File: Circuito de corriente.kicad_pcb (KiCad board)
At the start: 2 copper layers, 150 x 120 mm, 110 parts, among them J1 SALIDAS, J2 ENTRADAS, J3 +12V2, J4 +3V3, J5 +/- 5V, J6 +/- 12V, J7 INPUT_CEDCp, K1 JJM1-12V, K2 JJM1-12V, K3 JJM1-12V, K4 SLA-12VDC-SL-C, M1 Fan_3pin, Q1 BC337, Q2 BC327, U1 OPA604, U13 LM35-NEB, U16 Fuse, U18 IRLZ44N, U2 OPA604, U20 IRLZ44N, U22 IRLZ44N, U3 A6841, U4 AD7606_M, U5 MCP4725, U55 IRLZ44N, U6 OPA604, U7 OPA604, U8 OPA604

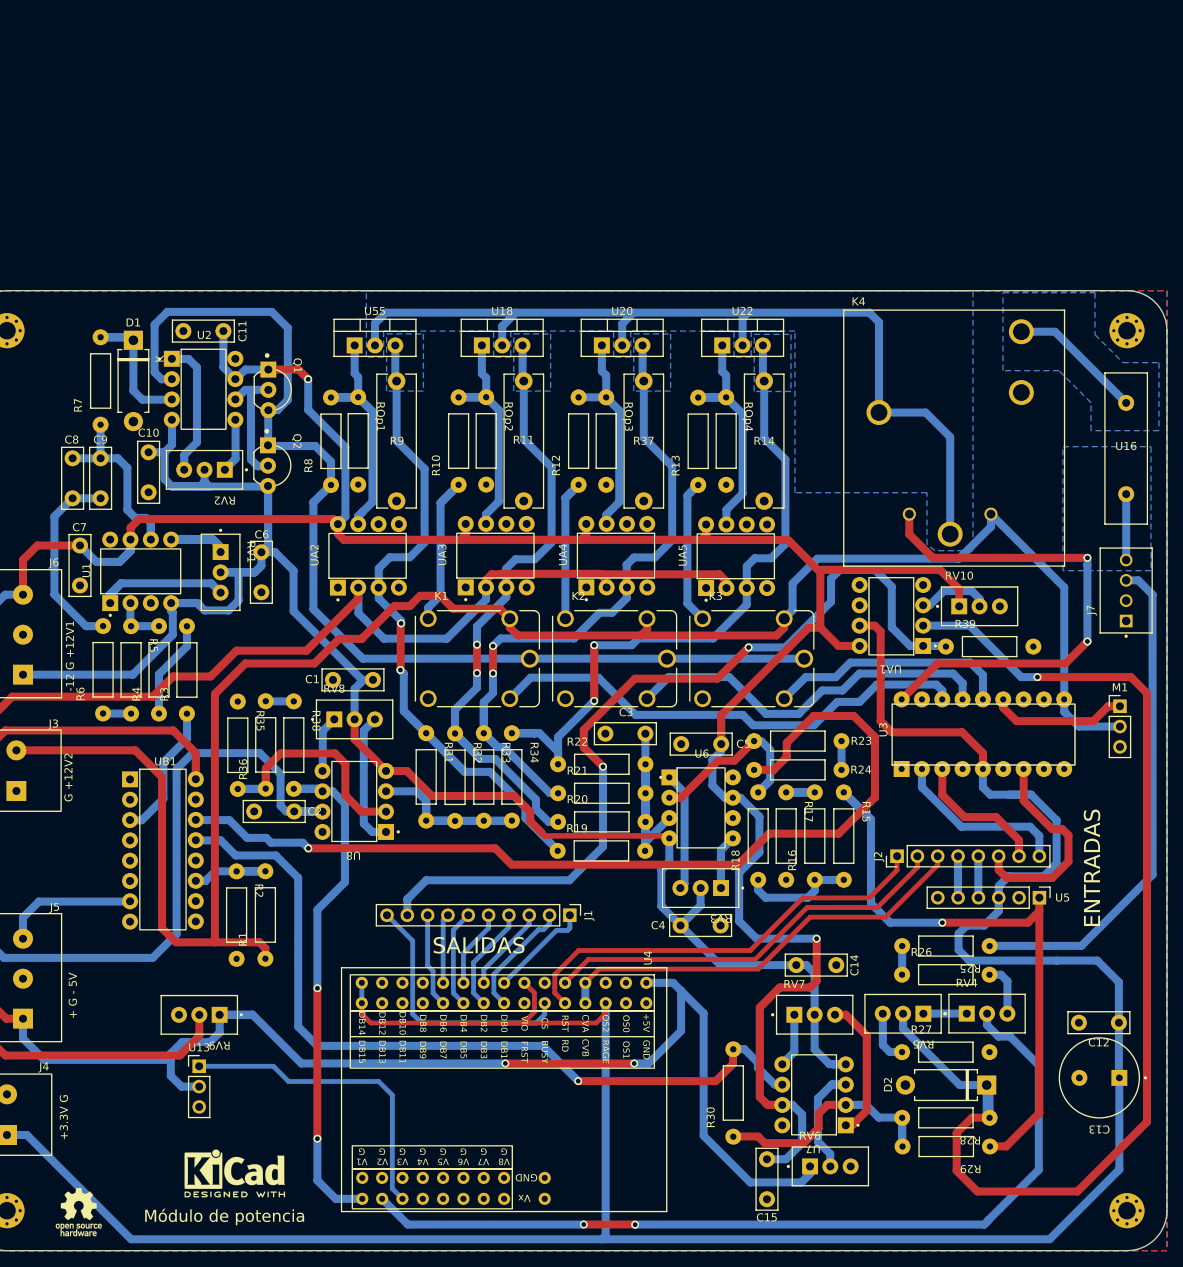
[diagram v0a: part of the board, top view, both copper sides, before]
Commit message: Heat sink added + Large pads
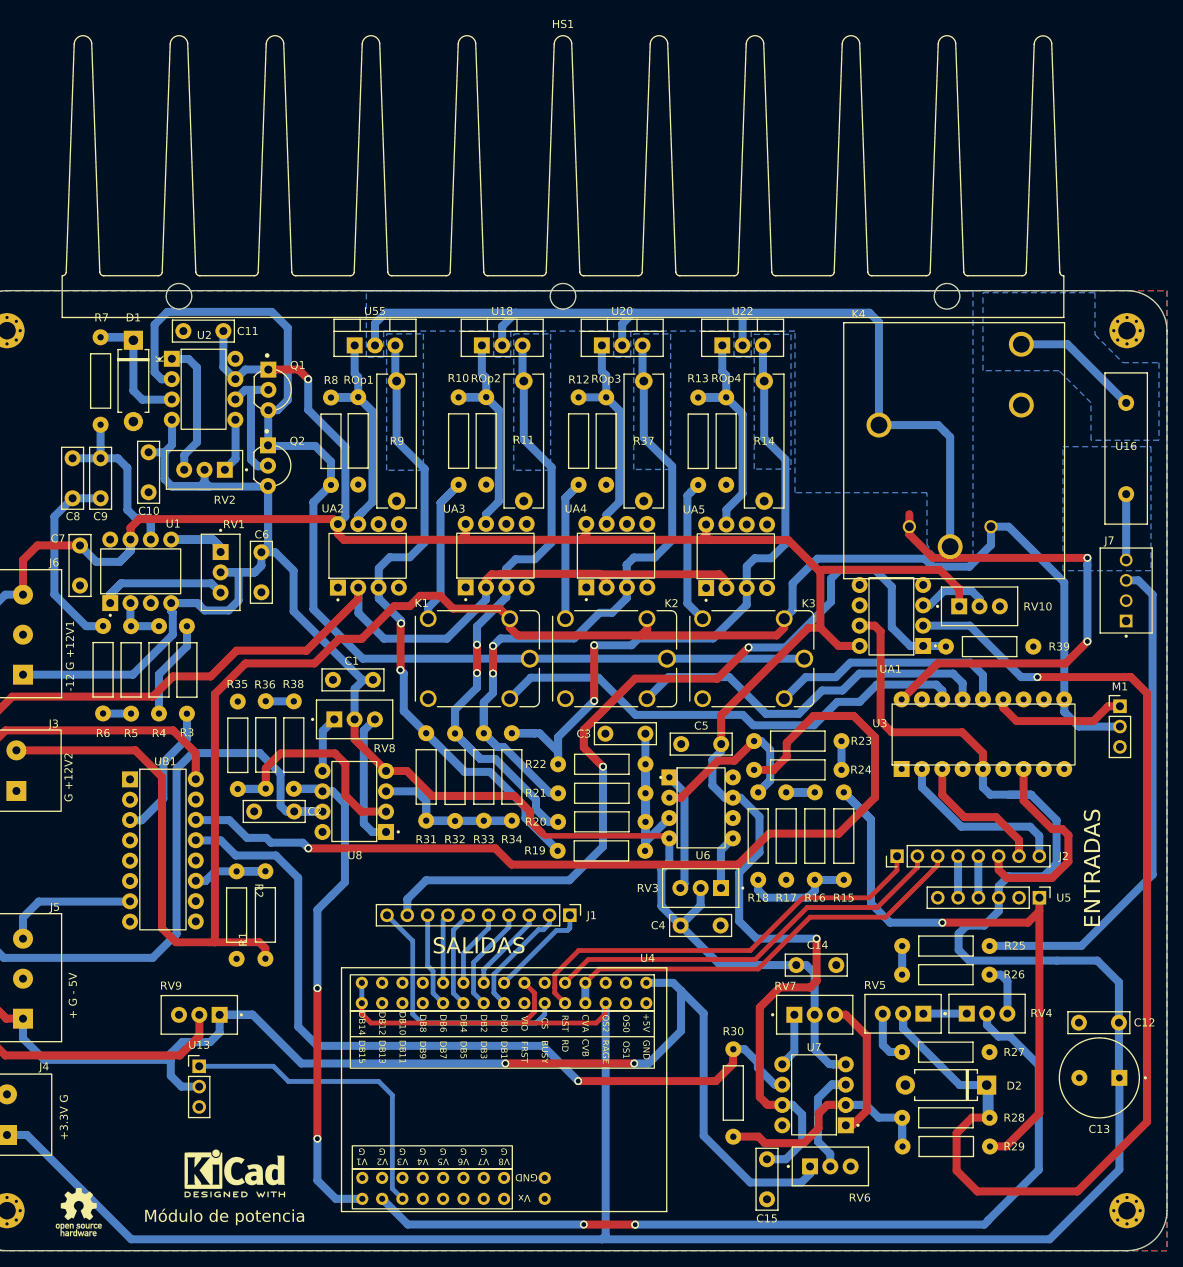
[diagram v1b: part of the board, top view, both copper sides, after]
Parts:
- added HS1: Heatsink, Heatsink:Heatsink_125x35x50mm_3xFixationM3, F.Cu at (139.7, 28.4)
- moved K4 1.57 mm to (188.1, 42.0)
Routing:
- net /CEP_Input+_MOS: track 114.2 -> 115.2 mm
- net /Proteccion Sobre Tension (53V)/F_In: track 16.8 -> 16.1 mm

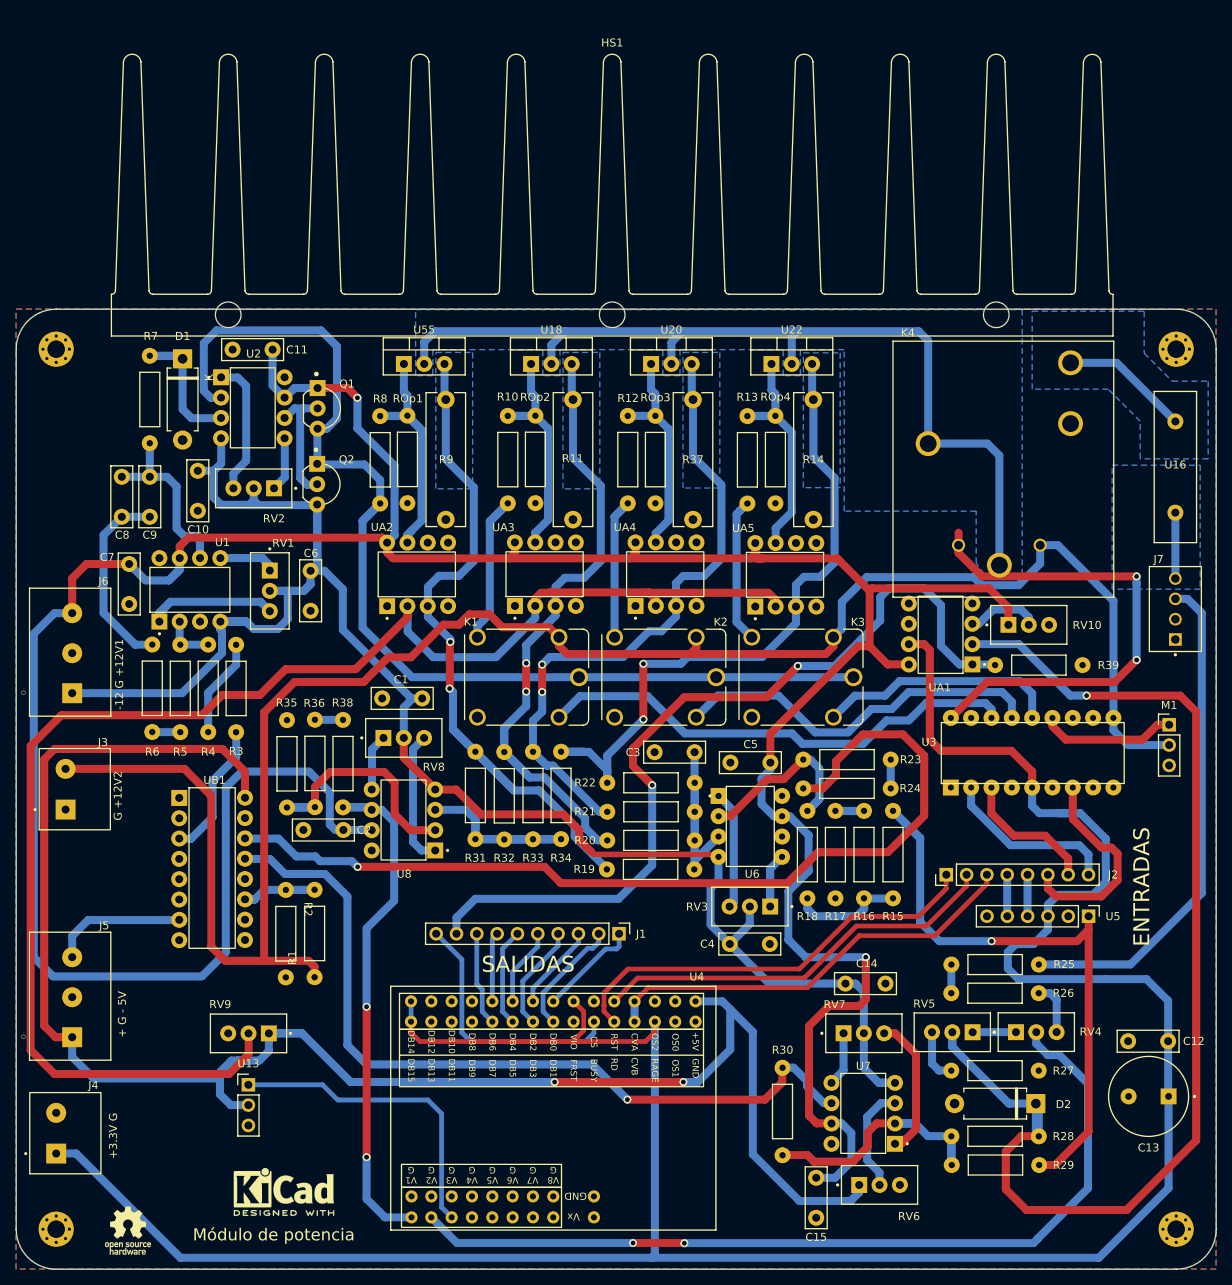
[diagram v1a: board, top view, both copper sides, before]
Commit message: Pads mas grandes y correccion de vias
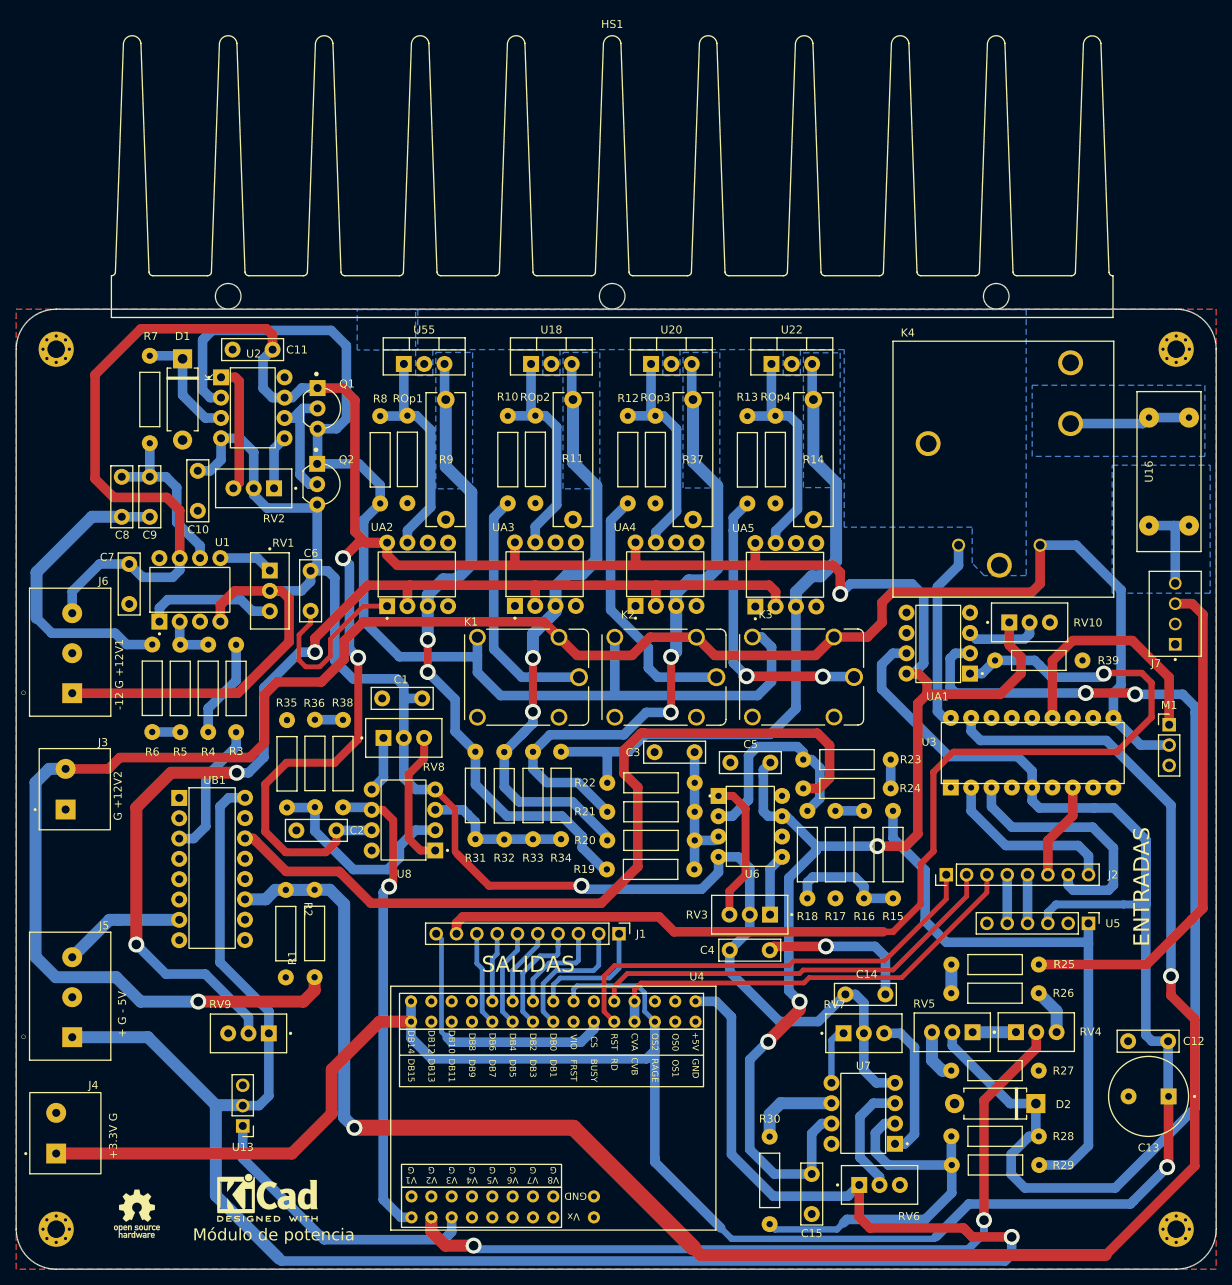
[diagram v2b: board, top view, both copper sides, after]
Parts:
- U16: footprint Fuse:Fuse_Littelfuse-LVR100 -> CEDCp:Fuse
- moved R30 8.76 mm to (159.4, 136.6)
- moved U13 5.19 mm to (93.5, 129.8), turned to 180 degrees
- moved U16 3.67 mm to (206.8, 54.8)
- moved REF** 2.39 mm to (80.3, 140.8)
- moved HS1 2.31 mm to (139.7, 26.1)
- moved REF** 2.20 mm to (96.6, 138.8)
- moved C14 1.35 mm to (173.8, 113.3)
- moved UA1 1.18 mm to (180.5, 69.4)
- moved RV3 1.01 mm to (156.9, 103.4)
- moved U5 0.89 mm to (199.2, 104.5)
- moved C2 0.88 mm to (100.2, 92.8)
- moved C4 0.77 mm to (154.4, 107.8)
- moved C15 0.73 mm to (164.6, 140.8)
- moved J7 0.60 mm to (210.1, 69.6)
- moved R39 0.59 mm to (193.0, 71.6)
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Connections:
- K1 pad 3: Net-(K1-Pad3) -> /PushPullOut
- K1 pad 5: /PushPullOut -> Net-(K1-Pad5)
- K2 pad 3: Net-(K2-Pad3) -> /PushPullOut
- K2 pad 5: /PushPullOut -> Net-(R12-Pad1)
- K3 pad 3: Net-(K3-Pad3) -> /PushPullOut
- K3 pad 5: /PushPullOut -> Net-(R13-Pad1)
- K4 pad NC: /Proteccion Sobre Tension (53V)/F_In -> unconnected-(K4-PadNC)
- K4 pad NO: GND -> /Proteccion Sobre Tension (53V)/F_In
- R1 pad 2: /fromMicroC_FBLSelection -> /fromA6841_FeedbackLoopSelection
- R10 pad 1: Net-(K1-Pad3) -> Net-(K1-Pad5)
- R12 pad 1: Net-(K2-Pad3) -> Net-(R12-Pad1)
- R13 pad 1: Net-(K3-Pad3) -> Net-(R13-Pad1)
- R2 pad 1: /fromMicroC_FBLSelection -> /fromA6841_FeedbackLoopSelection
- UB1 pad 11: /fromMicroC_FBLSelection -> /fromA6841_FeedbackLoopSelection
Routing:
- net /fromA6841_FeedbackLoopSelection: track 0.00 -> 261.4 mm, vias 0 -> 2
- net /CEP_Input+_MOS: track 115.2 -> 0.00 mm
- net /Error2: track 101.6 -> 11.1 mm, vias 1 -> 0
- net Net-(K1-Pad2): track 61.1 -> 0.00 mm
- net Net-(U3-Pad15): track 47.1 -> 0.00 mm
- net GND: track 0.00 -> 46.1 mm, vias 0 -> 1
- net /+5V: track 220.4 -> 260.0 mm, vias 2 -> 1
- net /ILimit_Vref: track 183.9 -> 144.6 mm, vias 0 -> 4
- net /fromA6841_PowerEnable: track 62.7 -> 23.9 mm, vias 2 -> 0
- net Net-(R13-Pad1): track 0.00 -> 36.5 mm, vias 0 -> 2
- net /toMicroC_OverVoltageSignal: track 107.0 -> 140.7 mm, vias 2 -> 1
- net Net-(R12-Pad1): track 0.00 -> 32.4 mm
- net Net-(K1-Pad5): track 0.00 -> 31.1 mm
- net Net-(U3-Pad14): track 30.4 -> 0.00 mm
- net Net-(K1-Pad3): track 21.5 -> 0.00 mm
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
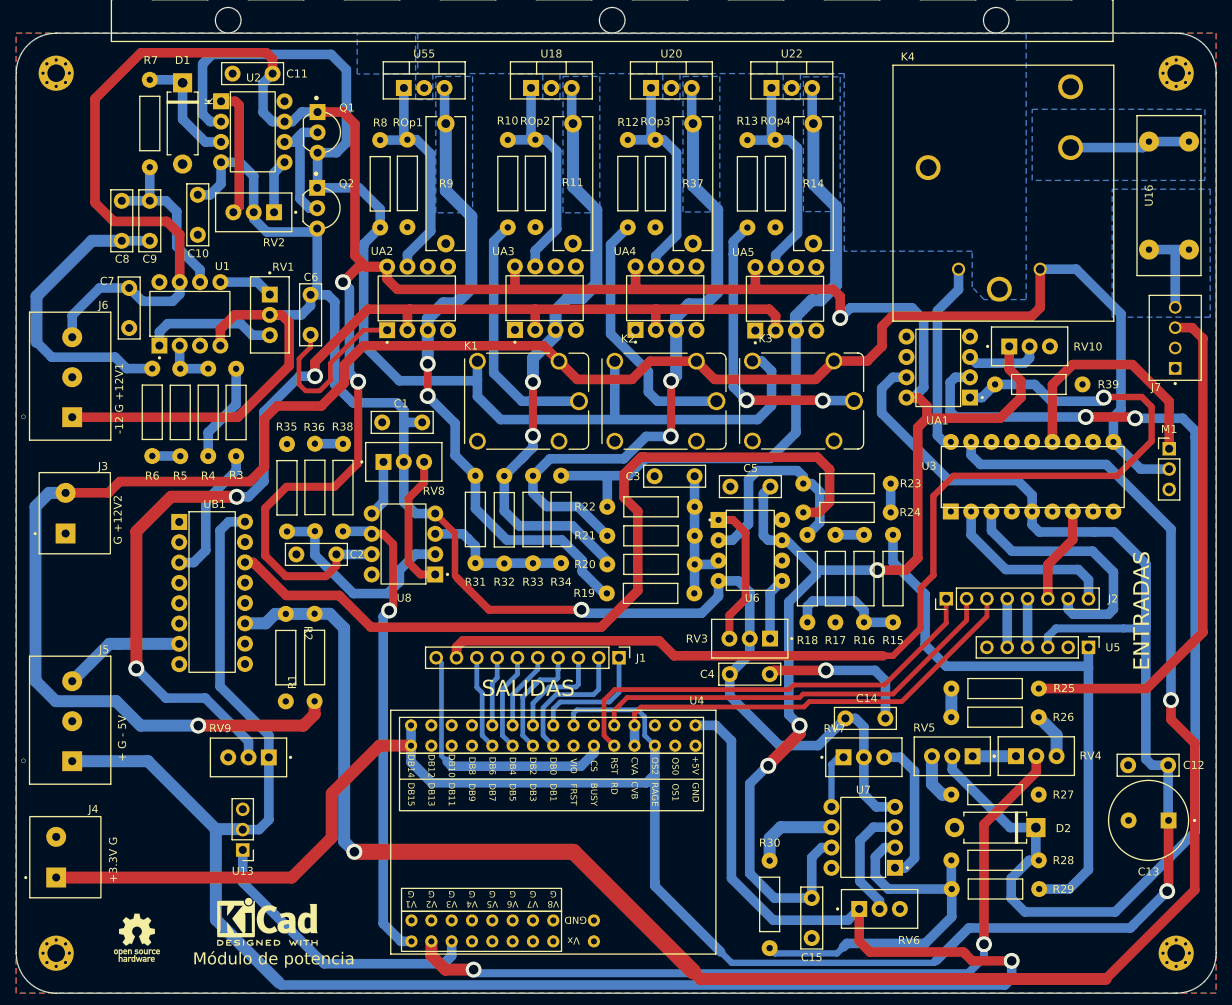
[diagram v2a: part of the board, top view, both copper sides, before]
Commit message: Se agrandaron los pads de las VIAS y ensancharon las pistas
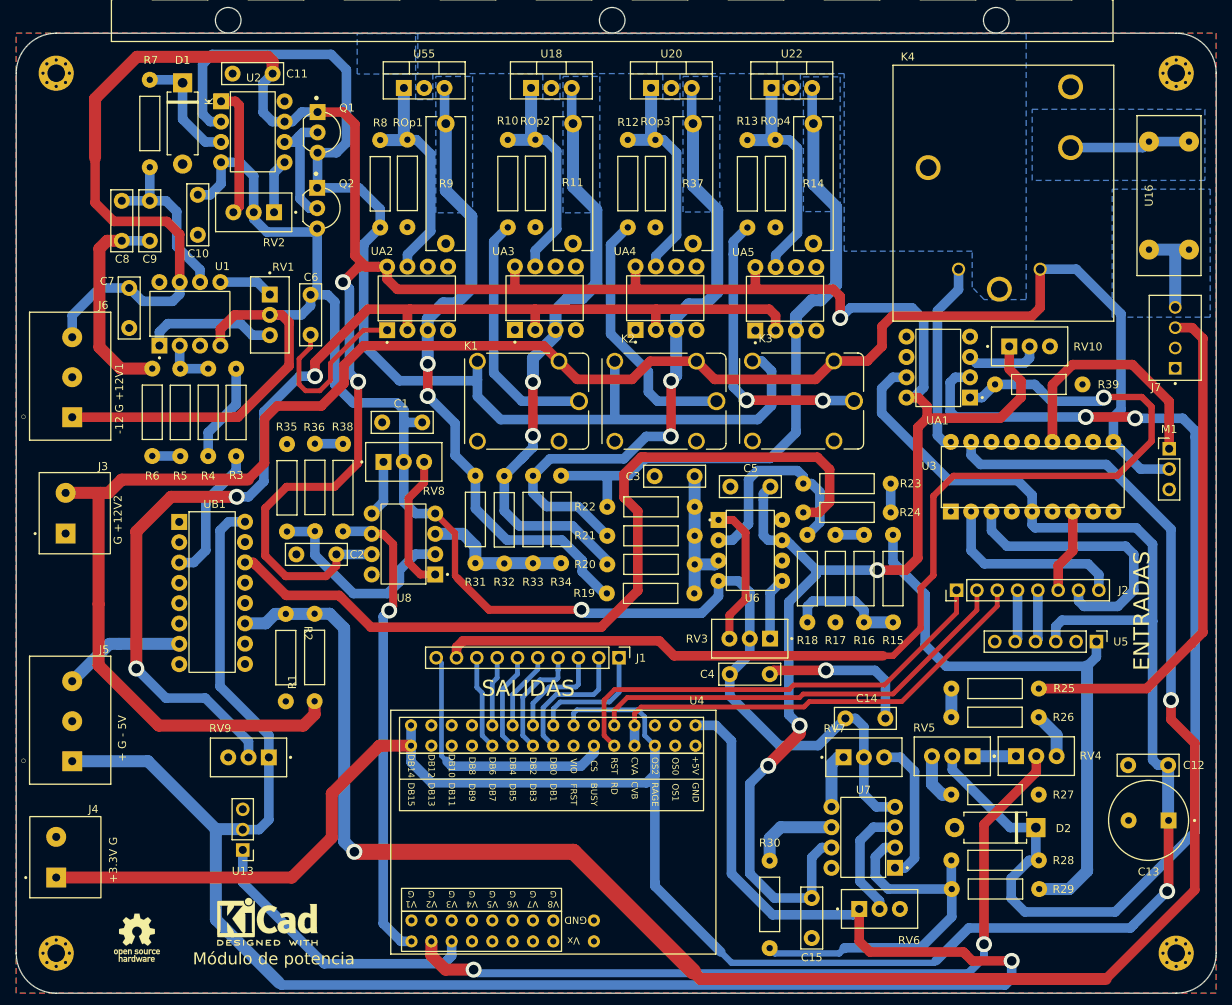
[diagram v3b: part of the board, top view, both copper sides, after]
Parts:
- moved J2 1.67 mm to (182.8, 97.3)
- moved U5 1.22 mm to (200.2, 103.8)
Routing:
- net /+3.3V: track 352.0 -> 315.8 mm
- net Net-(C8-Pad2): track 38.6 -> 26.7 mm
- net /CEP_Inpunt+_1: track 12.3 -> 17.3 mm
- net /+12V2: track 250.9 -> 247.2 mm, vias 1 -> 0
- net /fromDAC_Vref: track 73.3 -> 76.3 mm
- net /fromMicroC_A6841CLK1: track 22.3 -> 24.0 mm
- net /fromMicroC_ADC_CONV: track 55.3 -> 56.9 mm
- net /fromMicroC_A6841ST1: track 12.2 -> 10.6 mm
- net /fromMicroC_ADC_RST: track 53.3 -> 54.9 mm
- net /fromMicroC_ADC_RD: track 56.0 -> 57.6 mm
- net /+5V: track 260.0 -> 259.1 mm
- net /+12V1: track 414.9 -> 414.4 mm
